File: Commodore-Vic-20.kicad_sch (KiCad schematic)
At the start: 142 parts, among them CN1 Conn_01x03_Female, P1 User Port, P10 Keyboard, P2 CONN_Cassette, P3 SERIAL, P4 Audio / Video, P5 Controller Port, P6 Expansion Port, P7 POWER, Q1 2SC1815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

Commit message: refresh project details
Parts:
- removed C17: 47u, Capacitor_THT:C_Disc_D4.7mm_W2.5mm_P5.00mm, symbol Device:C_Small
- removed C7: 2u2, Capacitor_THT:C_Disc_D4.7mm_W2.5mm_P5.00mm, symbol Device:C_Small
- added C14: 47u, Commodore:CP_Radial_D5.0mm_P5.0mm, symbol Device:C_Polarized_Small
- added C7: 2u2, Capacitor_THT:CP_Radial_D5.0mm_P2.50mm, symbol Commodore-Vic-20-rescue:CP-Device
- C4: footprint Commodore:CP_Radial_D5.0mm_P5.0mm -> Capacitor_THT:CP_Radial_D5.0mm_P2.50mm
- R41: footprint Resistor_THT:R_Axial_DIN0207_L6.3mm_D2.5mm_P10.16mm_Horizontal -> Resistor_THT:R_Axial_DIN0207_L6.3mm_D2.5mm_P5.08mm_Vertical
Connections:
- net +5V: now also C7.1
- net GND: now also C7.2
- net at C15.1, C16.1, FB9.2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: now also R11.1; no longer R11.2
- net at Q2.3 (B), R12.2: now also R11.2, C14.1; no longer R11.1
- net at R10.2: now also C14.2
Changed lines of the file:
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@@
   (junction (at 276.86 340.36) (diameter 0) (color 0 0 0 0)
   )
+  (junction (at 360.68 100.33) (diameter 0) (color 0 0 0 0)
+  )
   (junction (at 398.78 144.78) (diameter 0) (color 0 0 0 0)
   )
@@
   (junction (at 668.02 114.3) (diameter 0) (color 0 0 0 0)
   )
-  (junction (at 360.68 101.6) (diameter 0) (color 0 0 0 0)
-  )
   (junction (at 565.15 61.595) (diameter 0) (color 0 0 0 0)
   )
@@
   (junction (at 266.7 109.22) (diameter 0) (color 0 0 0 0)
   )
-  (junction (at 347.98 101.6) (diameter 0) (color 0 0 0 0)
-  )
   (junction (at 605.79 146.05) (diameter 0) (color 0 0 0 0)
   )
+  (junction (at 347.98 100.33) (diameter 0) (color 0 0 0 0)
+  )
   (junction (at 121.92 402.59) (diameter 0) (color 0 0 0 0)
   )
@@
     (stroke (width 0) (type default))
   )
-  (wire (pts (xy 417.195 165.735) (xy 421.005 165.735))
-    (stroke (width 0) (type default))
-  )
   (wire (pts (xy 228.6 191.77) (xy 238.76 191.77))
     (stroke (width 0) (type default))
@@
     (stroke (width 0) (type default))
   )
+  (wire (pts (xy 358.14 100.33) (xy 360.68 100.33))
+    (stroke (width 0) (type default))
+  )
   (bus (pts (xy 170.18 119.38) (xy 170.18 121.92))
     (stroke (width 0) (type default))
@@
     (stroke (width 0) (type default))
   )
-  (wire (pts (xy 356.87 101.6) (xy 360.68 101.6))
-    (stroke (width 0) (type default))
-  )
   (bus (pts (xy 798.83 71.12) (xy 798.83 73.66))
     (stroke (width 0) (type default))
@@
     (stroke (width 0) (type default))
   )
+  (wire (pts (xy 360.68 100.33) (xy 360.68 102.87))
+    (stroke (width 0) (type default))
+  )
   (wire (pts (xy 360.68 95.25) (xy 358.14 95.25))
     (stroke (width 0) (type default))
@@
     (stroke (width 0) (type default))
   )
-  (wire (pts (xy 410.21 165.735) (xy 412.115 165.735))
-    (stroke (width 0) (type default))
-  )
   (wire (pts (xy 214.63 331.47) (xy 214.63 340.995))
     (stroke (width 0) (type default))
@@
     (stroke (width 0) (type default))
   )
-  (wire (pts (xy 360.68 102.87) (xy 360.68 101.6))
-    (stroke (width 0) (type default))
-  )
   (bus (pts (xy 798.83 78.74) (xy 798.83 81.28))
     (stroke (width 0) (type default))
@@
     (stroke (width 0) (type default))
   )
+  (wire (pts (xy 347.98 100.33) (xy 347.98 102.87))
+    (stroke (width 0) (type default))
+  )
   (wire (pts (xy 801.37 78.74) (xy 806.45 78.74))
     (stroke (width 0) (type default))
@@
     (stroke (width 0) (type default))
   )
-  (wire (pts (xy 347.98 101.6) (xy 347.98 102.87))
-    (stroke (width 0) (type default))
-  )
   (bus (pts (xy 591.82 128.27) (xy 591.82 130.81))
     (stroke (width 0) (type default))
@@
     (stroke (width 0) (type default))
   )
-  (wire (pts (xy 351.79 101.6) (xy 347.98 101.6))
-    (stroke (width 0) (type default))
-  )
   (wire (pts (xy 612.14 161.29) (xy 612.14 165.1))
     (stroke (width 0) (type default))
@@
     (stroke (width 0) (type default))
   )
-  (wire (pts (xy 360.68 101.6) (xy 360.68 95.25))
+  (wire (pts (xy 360.68 95.25) (xy 360.68 100.33))
     (stroke (width 0) (type default))
   )
@@
     (stroke (width 0) (type default))
   )
+  (wire (pts (xy 415.29 165.735) (xy 421.005 165.735))
+    (stroke (width 0) (type default))
+  )
   (wire (pts (xy 109.22 347.98) (xy 170.18 347.98))
     (stroke (width 0) (type default))
@@
     (stroke (width 0) (type default))
   )
-  (wire (pts (xy 347.98 95.25) (xy 347.98 101.6))
+  (wire (pts (xy 347.98 95.25) (xy 347.98 100.33))
     (stroke (width 0) (type default))
   )
@@
     (stroke (width 0) (type default))
   )
+  (wire (pts (xy 347.98 100.33) (xy 350.52 100.33))
+    (stroke (width 0) (type default))
+  )
   (wire (pts (xy 284.48 490.22) (xy 284.48 487.68))
     (stroke (width 0) (type default))
@@
       (effects (font (size 1.27 1.27)) (justify left))
     )
-    (property "Footprint" "Commodore:CP_Radial_D5.0mm_P5.0mm" (at 211.1502 82.55 0)
+    (property "Footprint" "Capacitor_THT:CP_Radial_D5.0mm_P2.50mm" (at 211.1502 82.55 0)
       (effects (font (size 1.27 1.27)) hide)
     )
@@
     )
   )
-  (symbol (lib_id "Device:C_Small") (at 354.33 101.6 90) (unit 1)
-    (in_bom yes) (on_board yes) (dnp no)
-    (property "Reference" "C7" (at 355.6 104.14 90)
-      (effects (font (size 1.27 1.27)))
-    )
-    (property "Value" "2u2" (at 355.6 106.68 90)
-      (effects (font (size 1.27 1.27)))
-    )
-    (property "Footprint" "Capacitor_THT:C_Disc_D4.7mm_W2.5mm_P5.00mm" (at 354.33 101.6 0)
-      (effects (font (size 1.27 1.27)) hide)
-    )
-    (property "Datasheet" "~" (at 354.33 101.6 0)
-      (effects (font (size 1.27 1.27)) hide)
-    )
-    (pin "1")
-    (pin "2")
-    (instances
-      (project "Commodore-Vic-20"
-        (path "/12b7dc71-c774-4c36-b128-0efa0070fa41"
-          (reference "C7") (unit 1)
-        )
-      )
-    )
-  )
   (symbol (lib_id "Commodore-Vic-20-rescue:CP-Device") (at 354.33 95.25 90) (unit 1)
     (in_bom yes) (on_board yes) (dnp no)
@@
     )
   )
-  (symbol (lib_id "Device:R_US") (at 425.45 151.13 0) (mirror x) (unit 1)
+  (symbol (lib_id "Device:R_US") (at 425.45 151.13 0) (unit 1)
     (in_bom yes) (on_board yes) (dnp no)
-    (property "Reference" "R11" (at 430.53 152.4 0)
+    (property "Reference" "R11" (at 430.53 149.86 0)
       (effects (font (size 1.27 1.27)) (justify right))
     )
-    (property "Value" "1k8" (at 430.53 149.86 0)
+    (property "Value" "1k8" (at 430.53 152.4 0)
       (effects (font (size 1.27 1.27)) (justify right))
     )
-    (property "Footprint" "Resistor_THT:R_Axial_DIN0207_L6.3mm_D2.5mm_P5.08mm_Vertical" (at 426.466 150.876 90)
+    (property "Footprint" "Resistor_THT:R_Axial_DIN0207_L6.3mm_D2.5mm_P5.08mm_Vertical" (at 426.466 151.384 90)
       (effects (font (size 1.27 1.27)) hide)
     )
@@
     )
   )
-  (symbol (lib_id "Device:C_Small") (at 414.655 165.735 270) (unit 1)
-    (in_bom yes) (on_board yes) (dnp no)
-    (property "Reference" "C17" (at 417.195 161.925 90)
-      (effects (font (size 1.27 1.27)))
-    )
-    (property "Value" "47u" (at 417.195 163.83 90)
-      (effects (font (size 1.27 1.27)))
-    )
-    (property "Footprint" "Capacitor_THT:C_Disc_D4.7mm_W2.5mm_P5.00mm" (at 414.655 165.735 0)
-      (effects (font (size 1.27 1.27)) hide)
-    )
-    (property "Datasheet" "~" (at 414.655 165.735 0)
-      (effects (font (size 1.27 1.27)) hide)
-    )
-    (pin "1")
-    (pin "2")
-    (instances
-      (project "Commodore-Vic-20"
-        (path "/12b7dc71-c774-4c36-b128-0efa0070fa41"
-          (reference "C17") (unit 1)
-        )
-      )
-    )
-  )
   (symbol (lib_id "Commodore-Vic-20-rescue:CP_Small-Device") (at 302.26 287.02 0) (unit 1)
     (in_bom yes) (on_board yes) (dnp no)
@@
       (effects (font (size 1.27 1.27)) (justify right))
     )
-    (property "Footprint" "Resistor_THT:R_Axial_DIN0207_L6.3mm_D2.5mm_P10.16mm_Horizontal" (at 385.064 158.369 90)
+    (property "Footprint" "Resistor_THT:R_Axial_DIN0207_L6.3mm_D2.5mm_P5.08mm_Vertical" (at 385.064 158.369 90)
       (effects (font (size 1.27 1.27)) hide)
     )
@@
     )
   )
+  (symbol (lib_id "Commodore-Vic-20-rescue:CP-Device") (at 354.33 100.33 90) (mirror x) (unit 1)
+    (in_bom yes) (on_board yes) (dnp no)
+    (property "Reference" "C7" (at 355.6 106.68 90)
+      (effects (font (size 1.27 1.27)) (justify left))
+    )
+    (property "Value" "2u2" (at 356.87 104.14 90)
+      (effects (font (size 1.27 1.27)) (justify left))
+    )
+    (property "Footprint" "Capacitor_THT:CP_Radial_D5.0mm_P2.50mm" (at 358.14 101.2952 0)
+      (effects (font (size 1.27 1.27)) hide)
+    )
+    (property "Datasheet" "~" (at 354.33 100.33 0)
+      (effects (font (size 1.27 1.27)) hide)
+    )
+    (pin "1")
+    (pin "2")
+    (instances
+      (project "Commodore-Vic-20"
+        (path "/12b7dc71-c774-4c36-b128-0efa0070fa41"
+          (reference "C7") (unit 1)
+        )
+      )
+    )
+  )
   (symbol (lib_id "power:+5V") (at 718.566 224.282 0) (unit 1)
     (in_bom yes) (on_board yes) (dnp no)
@@
         )
       )
+    )
+  )
+  (symbol (lib_id "Device:C_Polarized_Small") (at 412.75 165.735 270) (unit 1)
+    (in_bom yes) (on_board yes) (dnp no) (fields_autoplaced)
+    (property "Reference" "C14" (at 413.2961 160.909 90)
+      (effects (font (size 1.27 1.27)))
+    )
+    (property "Value" "47u" (at 413.2961 163.449 90)
+      (effects (font (size 1.27 1.27)))
+    )
+    (property "Footprint" "Commodore:CP_Radial_D5.0mm_P5.0mm" (at 412.75 165.735 0)
+      (effects (font (size 1.27 1.27)) hide)
+    )
+    (property "Datasheet" "~" (at 412.75 165.735 0)
+      (effects (font (size 1.27 1.27)) hide)
+    )
+    (pin "1")
+    (pin "2")
+    (instances
+      (project "Commodore-Vic-20"
+        (path "/12b7dc71-c774-4c36-b128-0efa0070fa41"
+          (reference "C14") (unit 1)
+        )
+      )

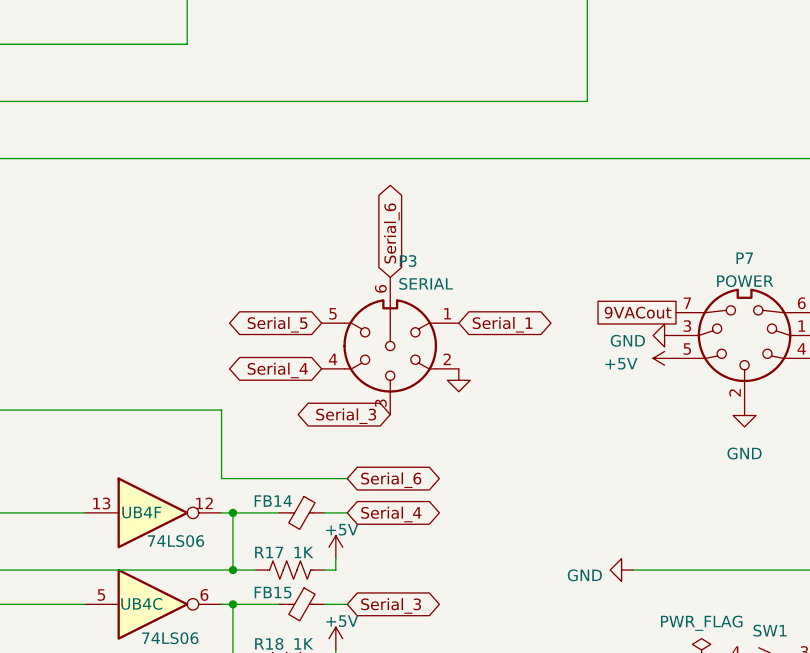
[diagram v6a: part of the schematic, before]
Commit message: improve trace names
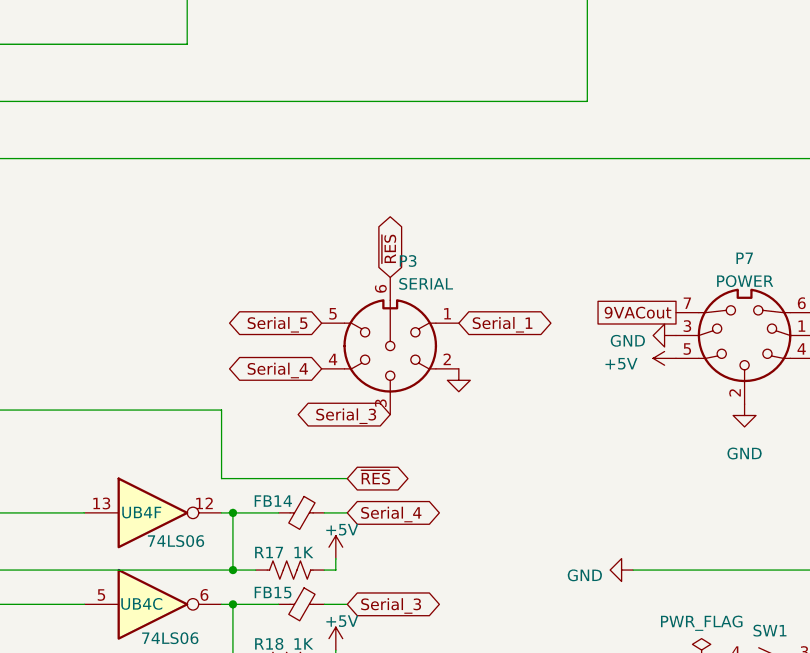
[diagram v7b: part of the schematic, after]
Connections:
- net Serial_6 renamed ~{RES}
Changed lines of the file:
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@@
     )
   )
-  (global_label "Serial_6" (shape bidirectional) (at 201.93 276.86 0) (fields_autoplaced)
+  (global_label "~{RES}" (shape bidirectional) (at 201.93 276.86 0) (fields_autoplaced)
     (effects (font (size 1.27 1.27)) (justify left))
-    (property "Intersheetrefs" "${INTERSHEET_REFS}" (at 212.8145 276.86 0)
+    (property "Intersheetrefs" "${INTERSHEET_REFS}" (at 208.7626 276.86 0)
       (effects (font (size 1.27 1.27)) (justify left) hide)
     )
@@
     )
   )
-  (global_label "Serial_6" (shape bidirectional) (at 206.7052 254.508 90) (fields_autoplaced)
+  (global_label "~{RES}" (shape bidirectional) (at 206.7052 254.508 90) (fields_autoplaced)
     (effects (font (size 1.27 1.27)) (justify left))
-    (property "Intersheetrefs" "${INTERSHEET_REFS}" (at 206.7052 243.6235 90)
+    (property "Intersheetrefs" "${INTERSHEET_REFS}" (at 206.7052 247.6754 90)
       (effects (font (size 1.27 1.27)) (justify left) hide)
     )

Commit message: progress traces
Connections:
- net at C36.1, CR2.3, L4.2: now also JP1.1 (Pin_1); no longer JP2.1 (Pin_1), P1.10 (+9V)
- net at C36.2, CR2.4, L4.4: now also JP1.2 (Pin_2); no longer JP2.2 (Pin_2), P1.11 (+9V)
- new net: JP2.1 (Pin_1), P1.10 (+9V)
- new net: JP2.2 (Pin_2), P1.11 (+9V)
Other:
- moved on the sheet: JP1
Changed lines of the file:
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@@
   (junction (at 425.45 144.78) (diameter 0) (color 0 0 0 0)
   )
-  (junction (at 171.45 438.15) (diameter 0) (color 0 0 0 0)
-  )
   (junction (at 668.02 114.3) (diameter 0) (color 0 0 0 0)
   )
@@
   (junction (at 105.41 40.64) (diameter 0) (color 0 0 0 0)
   )
-  (junction (at 173.99 440.69) (diameter 0) (color 0 0 0 0)
-  )
   (junction (at 190.5 313.69) (diameter 0) (color 0 0 0 0)
   )
@@
     (stroke (width 0) (type default))
   )
+  (wire (pts (xy 171.704 451.358) (xy 171.704 461.01))
+    (stroke (width 0) (type default))
+  )
   (bus (pts (xy 707.39 40.64) (xy 707.39 71.12))
     (stroke (width 0) (type default))
@@
     (stroke (width 0) (type default))
   )
-  (wire (pts (xy 212.09 373.38) (xy 187.96 373.38))
+  (wire (pts (xy 211.836 373.38) (xy 187.96 373.38))
     (stroke (width 0) (type default))
   )
@@
     (stroke (width 0) (type default))
   )
-  (wire (pts (xy 171.45 438.15) (xy 179.07 438.15))
+  (wire (pts (xy 170.688 438.15) (xy 179.07 438.15))
     (stroke (width 0) (type default))
   )
@@
     (stroke (width 0) (type default))
   )
-  (wire (pts (xy 214.63 370.84) (xy 214.63 463.55))
+  (wire (pts (xy 214.63 370.84) (xy 214.63 463.042))
     (stroke (width 0) (type default))
   )
@@
     (stroke (width 0) (type default))
   )
-  (wire (pts (xy 173.99 440.69) (xy 179.07 440.69))
+  (wire (pts (xy 170.688 440.69) (xy 179.07 440.69))
     (stroke (width 0) (type default))
   )
@@
     (stroke (width 0) (type default))
   )
-  (wire (pts (xy 212.09 373.38) (xy 212.09 461.01))
+  (wire (pts (xy 211.836 373.38) (xy 211.836 461.01))
     (stroke (width 0) (type default))
   )
@@
     (stroke (width 0) (type default))
   )
-  (wire (pts (xy 173.99 440.69) (xy 173.99 461.01))
+  (wire (pts (xy 170.18 451.358) (xy 171.704 451.358))
     (stroke (width 0) (type default))
   )
@@
     (stroke (width 0) (type default))
   )
-  (wire (pts (xy 171.45 438.15) (xy 171.45 463.55))
-    (stroke (width 0) (type default))
-  )
   (wire (pts (xy 243.205 324.485) (xy 229.87 324.485))
     (stroke (width 0) (type default))
@@
     (stroke (width 0) (type default))
   )
-  (wire (pts (xy 173.99 461.01) (xy 212.09 461.01))
+  (wire (pts (xy 171.704 461.01) (xy 211.836 461.01))
     (stroke (width 0) (type default))
   )
@@
     (stroke (width 0) (type default))
   )
+  (wire (pts (xy 170.18 453.898) (xy 170.18 463.042))
+    (stroke (width 0) (type default))
+  )
   (wire (pts (xy 255.27 75.565) (xy 254 75.565))
     (stroke (width 0) (type default))
@@
     (stroke (width 0) (type default))
   )
-  (wire (pts (xy 214.63 463.55) (xy 171.45 463.55))
+  (wire (pts (xy 214.63 463.042) (xy 170.18 463.042))
     (stroke (width 0) (type default))
   )
@@
     (stroke (width 0) (type default))
   )
-  (wire (pts (xy 170.688 440.69) (xy 173.99 440.69))
-    (stroke (width 0) (type default))
-  )
   (wire (pts (xy 647.7 60.96) (xy 647.7 69.85))
     (stroke (width 0) (type default))
@@
     (stroke (width 0) (type default))
   )
-  (wire (pts (xy 170.688 438.15) (xy 171.45 438.15))
-    (stroke (width 0) (type default))
-  )
   (wire (pts (xy 624.84 175.26) (xy 629.92 175.26))
     (stroke (width 0) (type default))
@@
     )
   )
-  (symbol (lib_id "Connector:Conn_01x02_Socket") (at 344.424 310.134 0) (unit 1)
+  (symbol (lib_id "Connector:Conn_01x02_Socket") (at 165.1 453.898 180) (unit 1)
     (in_bom yes) (on_board yes) (dnp no) (fields_autoplaced)
-    (property "Reference" "JP1" (at 345.186 310.769 0)
-      (effects (font (size 1.27 1.27)) (justify left))
+    (property "Reference" "JP1" (at 165.735 447.04 0)
+      (effects (font (size 1.27 1.27)))
     )
-    (property "Value" "power" (at 345.186 313.309 0)
-      (effects (font (size 1.27 1.27)) (justify left))
+    (property "Value" "power" (at 165.735 449.58 0)
+      (effects (font (size 1.27 1.27)))
     )
-    (property "Footprint" "Connector_PinSocket_2.54mm:PinSocket_1x02_P2.54mm_Vertical" (at 344.424 310.134 0)
+    (property "Footprint" "Connector_PinSocket_2.54mm:PinSocket_1x02_P2.54mm_Vertical" (at 165.1 453.898 0)
       (effects (font (size 1.27 1.27)) hide)
     )
-    (property "Datasheet" "~" (at 344.424 310.134 0)
+    (property "Datasheet" "~" (at 165.1 453.898 0)
       (effects (font (size 1.27 1.27)) hide)
     )
